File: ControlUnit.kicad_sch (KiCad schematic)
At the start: 14 parts, among them U27 74LS163, U28 AT28C64B, U29 AT28C64B, U30 AT28C64B, U31 74LS08, U32 74LS32, U33 74LS74

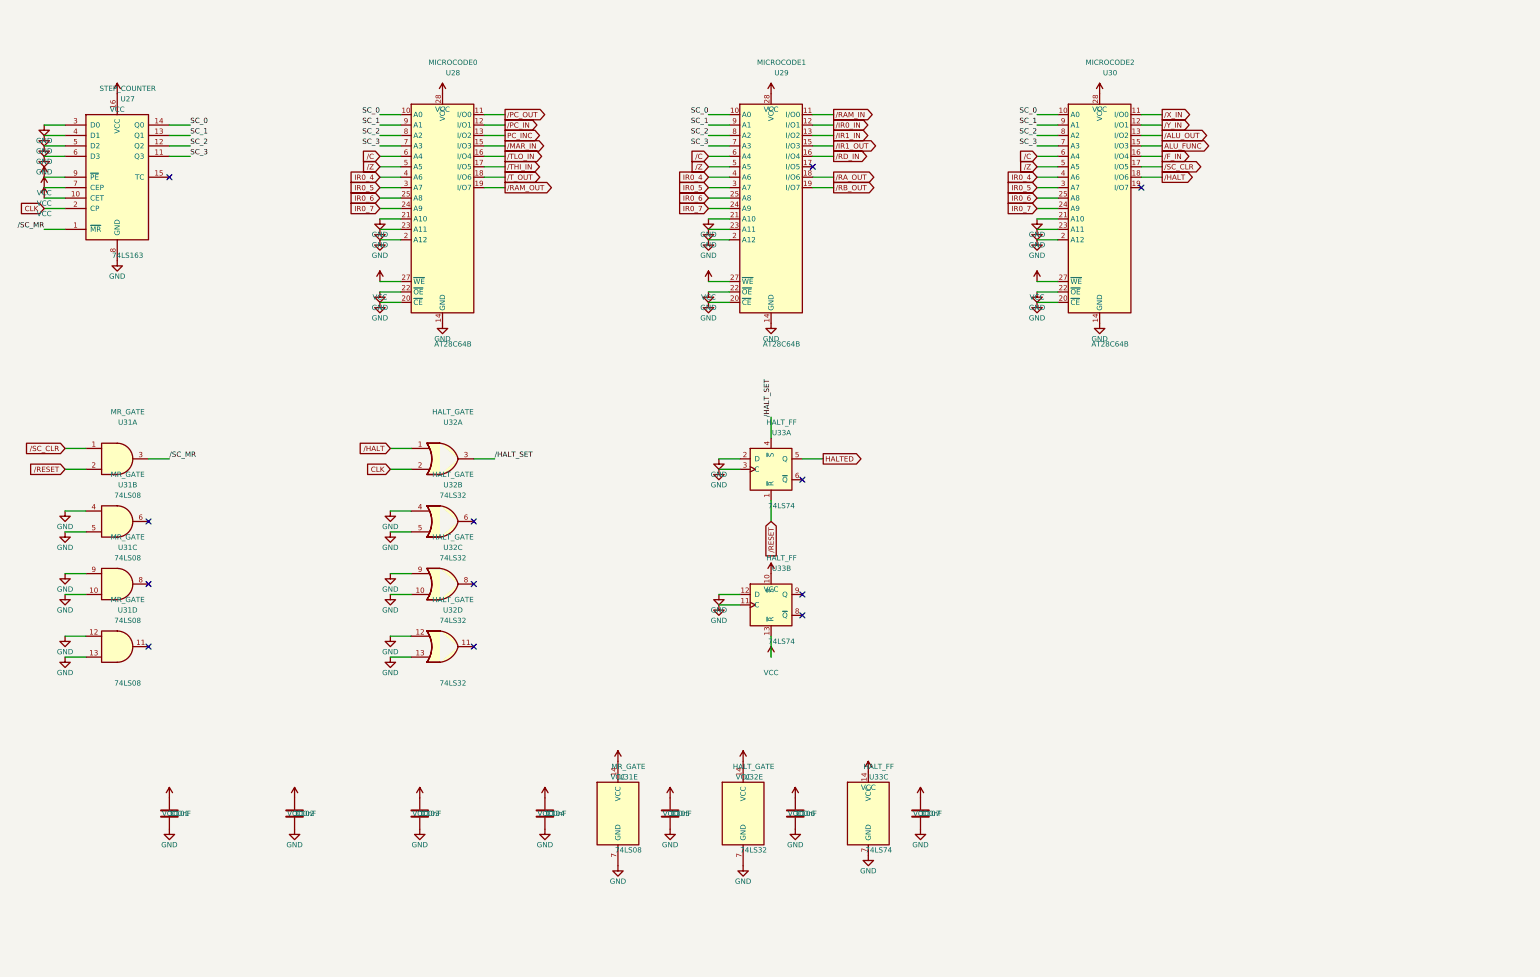
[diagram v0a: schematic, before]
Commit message: Cleans up and restructures schematics
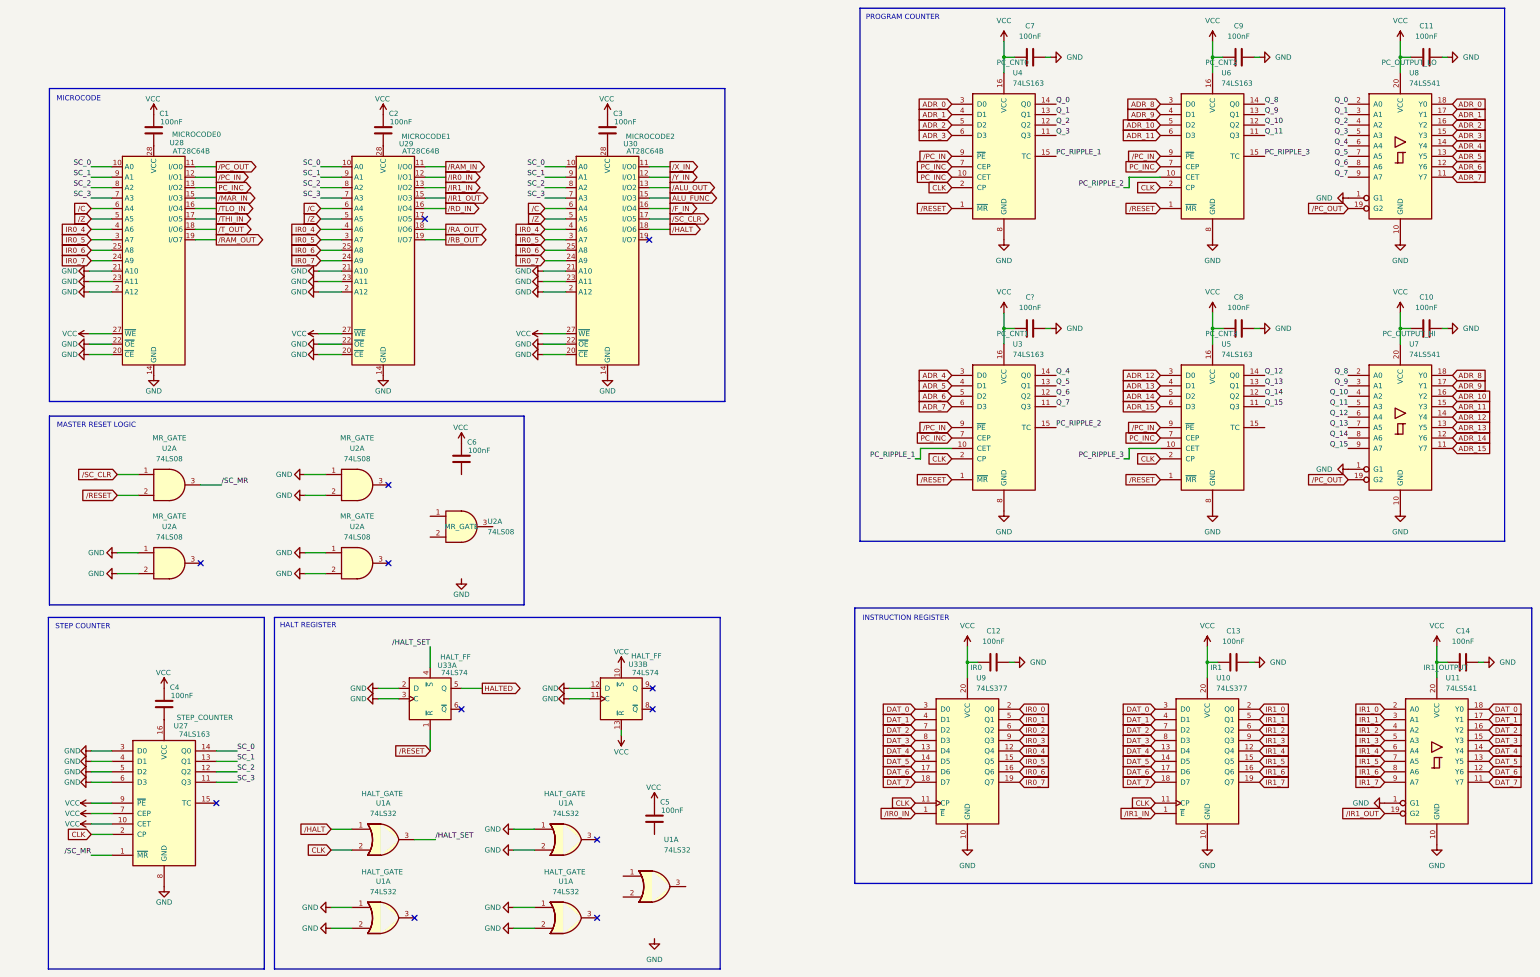
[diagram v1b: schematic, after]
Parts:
- removed C101, C102, C103, C104, C105, C106, C107: 100nF, Capacitor_THT:C_Disc_D5.0mm_W2.5mm_P5.00mm, symbol Device:C
- removed U31: 74LS08, Package_DIP:DIP-14_W7.62mm, symbol 74xx:74LS08
- removed U32: 74LS32, Package_DIP:DIP-14_W7.62mm, symbol 74xx:74LS32
- removed unit 3 of U33
- added C1, C10, C11, C12, C13, C14, C2, C3, C4, C5, C6, C7, C8, C9, C?: 100nF, Capacitor_THT:C_Disc_D5.0mm_W2.5mm_P5.00mm, symbol Device:C
- added U1 (x5): 74LS32, symbol 74xx:74LS32
- added U10, U9: 74LS377, Package_DIP:DIP-20_W7.62mm, symbol 74xx:74LS377
- added U11, U7, U8: 74LS541, Package_DIP:DIP-20_W7.62mm, symbol 74xx:74LS541
- added U2 (x5): 74LS08, symbol 74xx:74LS08
- added U3, U4, U5, U6: 74LS163, Package_DIP:DIP-16_W7.62mm, symbol 74xx:74LS163
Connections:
- net CLK: now also U1.2, U10.11 (CP), U3.2 (CP), U4.2 (CP), U5.2 (CP), U6.2 (CP), U9.11 (CP)
- net GND: now also C10.2, C11.2, C12.2, C13.2, C14.2, C7.2, C8.2, C9.2, C?.2, U1.1, U1.1, U1.1, U1.2, U1.2, U1.2, U10.10 (GND), U11.1 (G1), U11.10 (GND), U2.1, U2.1, U2.1, U2.2, U2.2, U2.2, U3.8 (GND), U4.8 (GND), U5.8 (GND), U6.8 (GND), U7.1 (G1), U7.10 (GND), U8.1 (G1), U8.10 (GND), U9.10 (GND)
- net IR0_4: now also U9.12 (Q4)
- net IR0_5: now also U9.15 (Q5)
- net IR0_6: now also U9.16 (Q6)
- net IR0_7: now also U9.19 (Q7)
- net PC_INC: now also U3.7 (CEP), U4.10 (CET), U4.7 (CEP), U5.7 (CEP), U6.7 (CEP)
- net VCC: now also C1.1, C10.1, C11.1, C12.1, C13.1, C14.1, C2.1, C3.1, C4.1, C5.1, C6.1, C7.1, C8.1, C9.1, C?.1, U10.20 (VCC), U11.20 (VCC), U3.16 (VCC), U4.16 (VCC), U5.16 (VCC), U6.16 (VCC), U7.20 (VCC), U8.20 (VCC), U9.20 (VCC); no longer U27.16 (VCC), U28.28 (VCC), U29.28 (VCC), U30.28 (VCC)
- net /HALT: now also U1.1
- net /HALT_SET: now also U1.3
- net /IR0_IN: now also U9.1 (~{E})
- net /IR1_IN: now also U10.1 (~{E})
- net /IR1_OUT: now also U11.19 (G2)
- net /PC_IN: now also U3.9 (~{PE}), U4.9 (~{PE}), U5.9 (~{PE}), U6.9 (~{PE})
- net /PC_OUT: now also U7.19 (G2), U8.19 (G2)
- net /RESET: now also U2.2, U3.1 (~{MR}), U4.1 (~{MR}), U5.1 (~{MR}), U6.1 (~{MR})
- net /SC_CLR: now also U2.1
- net /SC_MR: now also U2.3
- new net: C2.2, U29.28 (VCC)
- new net: C1.2, U28.28 (VCC)
- new net: C4.2, U27.16 (VCC)
- new net: C3.2, U30.28 (VCC)
- new net ADR_0: U4.3 (D0), U8.18 (Y0)
- new net ADR_1: U4.4 (D1), U8.17 (Y1)
- new net ADR_10: U6.5 (D2), U7.16 (Y2)
- new net ADR_11: U6.6 (D3), U7.15 (Y3)
- new net ADR_12: U5.3 (D0), U7.14 (Y4)
- new net ADR_13: U5.4 (D1), U7.13 (Y5)
- new net ADR_14: U5.5 (D2), U7.12 (Y6)
- new net ADR_15: U5.6 (D3), U7.11 (Y7)
- new net ADR_2: U4.5 (D2), U8.16 (Y2)
- new net ADR_3: U4.6 (D3), U8.15 (Y3)
- new net ADR_4: U3.3 (D0), U8.14 (Y4)
- new net ADR_5: U3.4 (D1), U8.13 (Y5)
- new net ADR_6: U3.5 (D2), U8.12 (Y6)
- new net ADR_7: U3.6 (D3), U8.11 (Y7)
- new net ADR_8: U6.3 (D0), U7.18 (Y0)
- new net ADR_9: U6.4 (D1), U7.17 (Y1)
- new net DAT_0: U10.3 (D0), U11.18 (Y0), U9.3 (D0)
- new net DAT_1: U10.4 (D1), U11.17 (Y1), U9.4 (D1)
- new net DAT_2: U10.7 (D2), U11.16 (Y2), U9.7 (D2)
- new net DAT_3: U10.8 (D3), U11.15 (Y3), U9.8 (D3)
- new net DAT_4: U10.13 (D4), U11.14 (Y4), U9.13 (D4)
- new net DAT_5: U10.14 (D5), U11.13 (Y5), U9.14 (D5)
- new net DAT_6: U10.17 (D6), U11.12 (Y6), U9.17 (D6)
- new net DAT_7: U10.18 (D7), U11.11 (Y7), U9.18 (D7)
- new net IR0_0: U9.2 (Q0)
- new net IR0_1: U9.5 (Q1)
- new net IR0_2: U9.6 (Q2)
- new net IR0_3: U9.9 (Q3)
- new net IR1_0: U10.2 (Q0), U11.2 (A0)
- new net IR1_1: U10.5 (Q1), U11.3 (A1)
- new net IR1_2: U10.6 (Q2), U11.4 (A2)
- new net IR1_3: U10.9 (Q3), U11.5 (A3)
- new net IR1_4: U10.12 (Q4), U11.6 (A4)
- new net IR1_5: U10.15 (Q5), U11.7 (A5)
- new net IR1_6: U10.16 (Q6), U11.8 (A6)
- new net IR1_7: U10.19 (Q7), U11.9 (A7)
- new net PC_RIPPLE_1: U3.10 (CET), U4.15 (TC)
- new net PC_RIPPLE_2: U3.15 (TC), U6.10 (CET)
- new net PC_RIPPLE_3: U5.10 (CET), U6.15 (TC)
- new net Q_0: U4.14 (Q0), U8.2 (A0)
- new net Q_1: U4.13 (Q1), U8.3 (A1)
- new net Q_10: U6.12 (Q2), U7.4 (A2)
- new net Q_11: U6.11 (Q3), U7.5 (A3)
- new net Q_12: U5.14 (Q0), U7.6 (A4)
- new net Q_13: U5.13 (Q1), U7.7 (A5)
- new net Q_14: U5.12 (Q2), U7.8 (A6)
- new net Q_15: U5.11 (Q3), U7.9 (A7)
- new net Q_2: U4.12 (Q2), U8.4 (A2)
- new net Q_3: U4.11 (Q3), U8.5 (A3)
- new net Q_4: U3.14 (Q0), U8.6 (A4)
- new net Q_5: U3.13 (Q1), U8.7 (A5)
- new net Q_6: U3.12 (Q2), U8.8 (A6)
- new net Q_7: U3.11 (Q3), U8.9 (A7)
- new net Q_8: U6.14 (Q0), U7.2 (A0)
- new net Q_9: U6.13 (Q1), U7.3 (A1)
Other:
- note added: "HALT REGISTER"
- note added: "INSTRUCTION REGISTER"
- note added: "MASTER RESET LOGIC"
- note added: "MICROCODE"
- note added: "PROGRAM COUNTER"
- note added: "STEP COUNTER"
- moved on the sheet: U27, U28, U29, U30, U33A, U33B

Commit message: Fixes Gate symbol refs and adds backplane definition
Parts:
- renumbered U33 to U?, U29 to U?, U27 to U?, U30 to U?, U28 to U?
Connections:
- net GND: now also U1.10, U1.12, U1.13, U1.4, U1.5, U1.7 (GND), U1.9, U2.10, U2.12, U2.13, U2.4, U2.5, U2.7 (GND), U2.9, U?.2 (D), U?.3 (C); no longer U1.1, U1.1, U1.1, U1.2, U1.2, U1.2, U2.1, U2.1, U2.1, U2.2, U2.2, U2.2, U?.11 (C), U?.12 (D)
- net VCC: now also U?.1 (~{R}), U?.4 (~{S}); no longer U?.10 (~{S}), U?.13 (~{R})
- net at C5.2: now also U1.14 (VCC)
- net at C6.2: now also U2.14 (VCC)
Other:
- moved on the sheet: C10, C11, C12, C13, C14, C7, C8, C9, C?, U10, U11, U3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
